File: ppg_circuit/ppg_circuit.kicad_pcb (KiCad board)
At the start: 2 copper layers, 14 parts, among them U1 Opamp_Dual, U2 MCP6001x-LT

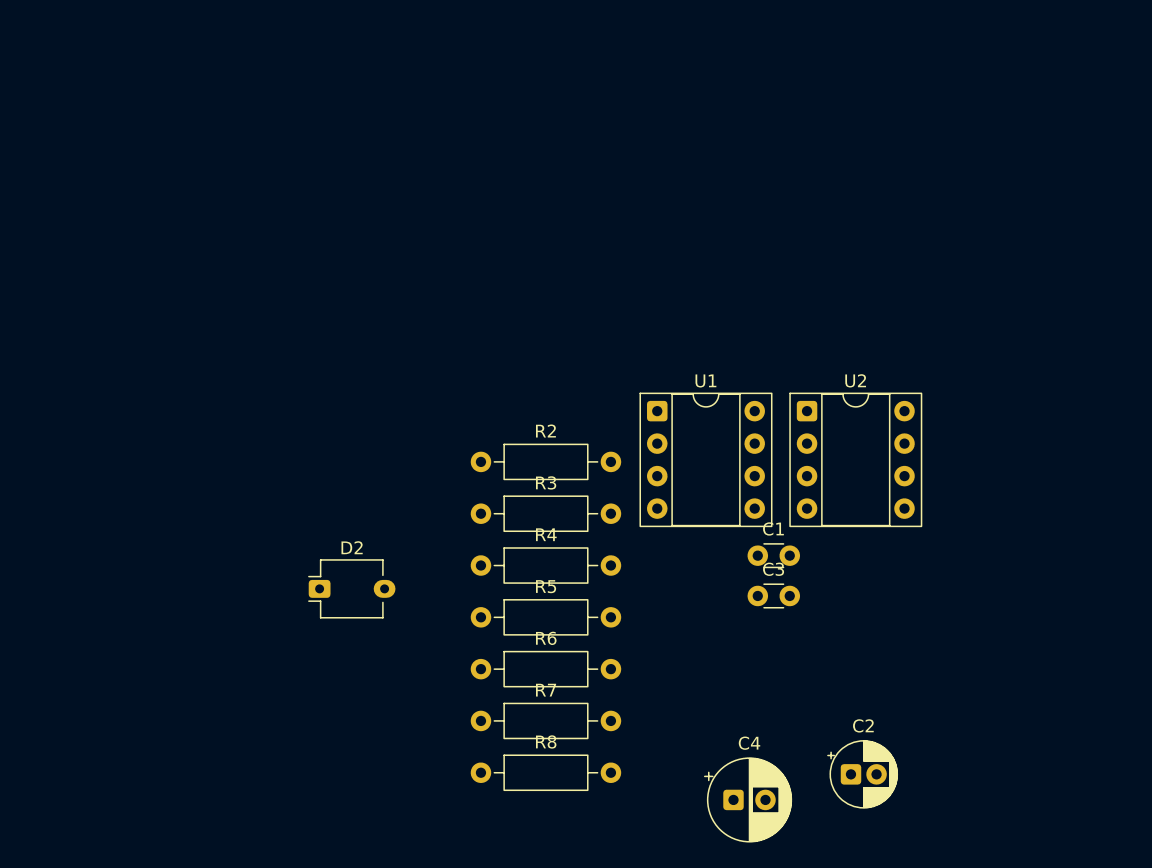
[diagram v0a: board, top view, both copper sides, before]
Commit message: designed pcb, added teensy to the design
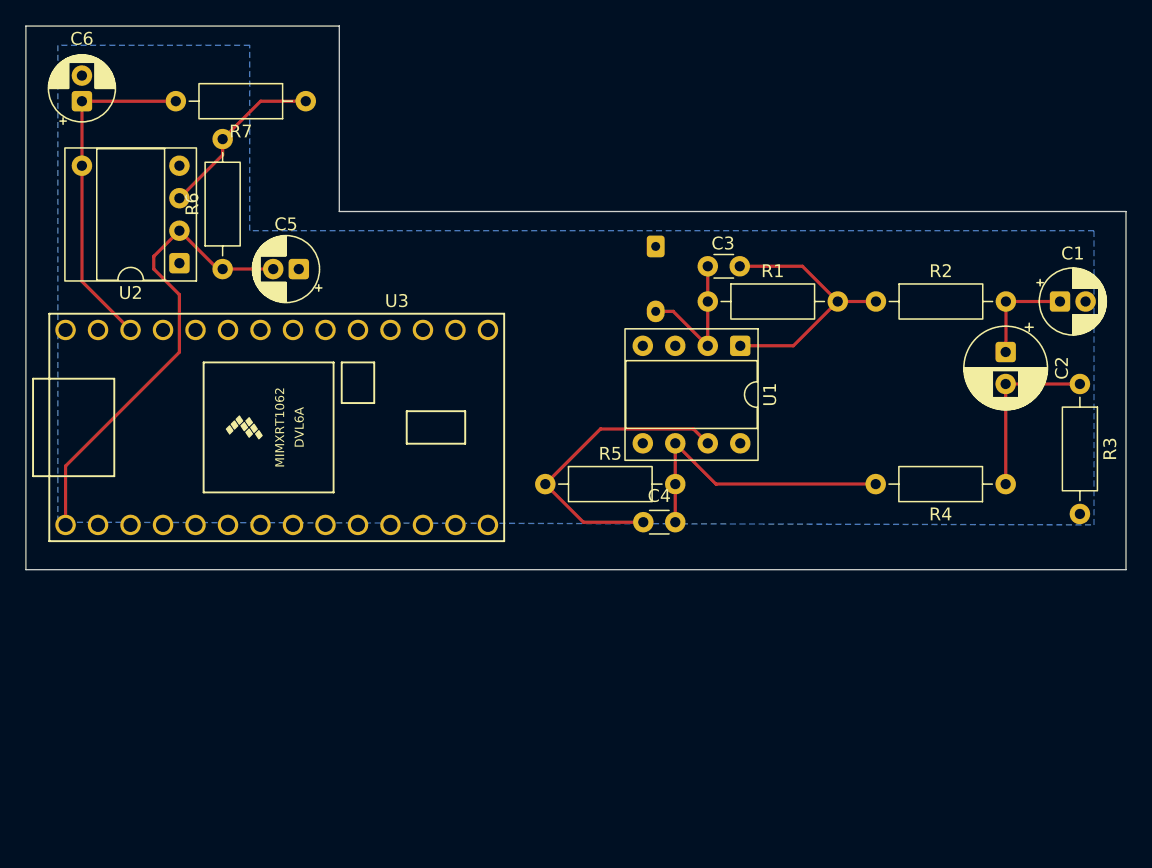
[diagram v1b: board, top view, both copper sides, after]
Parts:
- added C5: 10u, Capacitor_THT:CP_Radial_D5.0mm_P2.00mm, F.Cu at (62.3, 37.5)
- added C6: 10u, Capacitor_THT:CP_Radial_D5.0mm_P2.00mm, F.Cu at (45.4, 24.4)
- added U3: Teensy4.0, teensy:Teensy40, F.Cu at (60.6, 49.9)
- D1: renamed from D2; moved to B.Cu
- moved R7 54.3 mm to (62.9, 24.4), turned to 180 degrees
- moved U2 50.4 mm to (53.0, 37.0), turned to 180 degrees
- moved R3 50.2 mm to (123.4, 46.5), turned to -90 degrees
- moved R4 41.5 mm to (117.6, 54.3), turned to 180 degrees
- moved C2 41.0 mm to (117.6, 44.0), turned to -90 degrees
- moved R6 40.7 mm to (56.4, 37.5), turned to 90 degrees
- moved C1 40.4 mm to (121.8, 40.0)
- moved D1 37.5 mm to (90.2, 35.7), turned to -90 degrees
- moved R2 35.1 mm to (107.5, 40.0)
- moved C3 25.8 mm to (96.8, 37.3), turned to 180 degrees
- moved R1 21.7 mm to (94.3, 40.0)
- moved R5 15.3 mm to (81.6, 54.3)
- moved C4 9.32 mm to (89.3, 57.3)
- moved U1 8.26 mm to (96.8, 43.5), turned to -90 degrees
- renumbered C2 to C1, C4 to C2, C1 to C4, R2 to R1, R3 to R2, R5 to R3, R6 to R5, R7 to R6, R8 to R7
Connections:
- R6 pad 2: GND -> Net-(U2-+)
- R7 pad 1: GND -> Net-(U2-+)
- U2 pad 1: /ground -> GND
- U2 pad 3: GND -> Net-(U2-+)
- U2 pad 4: /ground -> GND
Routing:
- net /low: track 0.00 -> 36.9 mm
- net /high: track 0.00 -> 26.8 mm
- net /outf: track 0.00 -> 23.8 mm
- net Net-(U1B--): track 0.00 -> 23.2 mm
- net /out1: track 0.00 -> 20.8 mm
- net Net-(U2-+): track 0.00 -> 13.7 mm
- net /out3: track 0.00 -> 13.6 mm
- net /in: track 0.00 -> 11.4 mm
- net /out2: track 0.00 -> 8.19 mm
- added copper zone on B.Cu, net GND
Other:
- board outline added: 86 x 42.5 mm

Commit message: fixed errors in pcb and moved the photodiode so it is more accessable on the pcb
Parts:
- added REF**: MountingHole_2.2mm_M2, MountingHole:MountingHole_2.2mm_M2, F.Cu at (62.5, 29.0)
- moved D1 7.28 mm to (83.0, 35.5), turned to 0 degrees
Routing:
- net /low: track 36.9 -> 89.6 mm, vias 0 -> 1
- net /high: track 26.8 -> 78.1 mm, vias 0 -> 1
- net /outf: track 23.8 -> 38.8 mm
- net /in: track 11.4 -> 16.8 mm

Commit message: finished modular 3d design with 3 different components and added screw holes for fastening
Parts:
- removed the REF** at (62.5, 29.0)
- added REF**: MountingHole_2.2mm_M2, MountingHole:MountingHole_2.2mm_M2, F.Cu at (69.0, 37.0)
- added REF**: MountingHole_2.2mm_M2, MountingHole:MountingHole_2.2mm_M2, F.Cu at (117.5, 58.5)
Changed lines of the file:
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@@
 			(outputformat 1)
 			(mirror no)
-			(drillshape 1)
+			(drillshape 0)
 			(scaleselection 1)
-			(outputdirectory "")
+			(outputdirectory "gerber/")
 		)
 	)
@@
 		)
 	)
+	(footprint "MountingHole:MountingHole_2.2mm_M2"
+		(layer "F.Cu")
+		(at 69 37)
+		(descr "Mounting Hole 2.2mm, M2, no annular, generated by kicad-footprint-generator mountinghole.py")
+		(tags "mountinghole M2")
+		(property "Reference" "REF**"
+			(at 4.5 -2.5 0)
+			(layer "F.SilkS")
+			(effects
+				(font
+					(size 1 1)
+					(thickness 0.15)
+				)
+			)
+		)
+		(property "Value" "MountingHole_2.2mm_M2"
+			(at 0 3.15 0)
+			(layer "F.Fab")
+			(effects
+				(font
+					(size 1 1)
+					(thickness 0.15)
+				)
+			)
+		)
+		(property "Datasheet" ""
+			(at 0 0 0)
+			(layer "F.Fab")
+			(hide yes)
+			(effects
+				(font
+					(size 1.27 1.27)
+				)
+			)
+		)
+		(property "Description" ""
+			(at 0 0 0)
+			(layer "F.Fab")
+			(hide yes)
+			(effects
+				(font
+					(size 1.27 1.27)
+				)
+			)
+		)
+		(property "KiLib_Generator" "mounting_hardware/mounting_hole"
+			(at 0 0 0)
+			(layer "F.SilkS")
+			(hide yes)
+			(effects
+				(font
+					(size 1 1)
+					(thickness 0.15)
+				)
+			)
+		)
+		(attr exclude_from_pos_files exclude_from_bom)
+		(duplicate_pad_numbers_are_jumpers no)
+		(fp_circle
+			(center 0 0)
+			(end 2.2 0)
+			(stroke
+				(width 0.15)
+				(type solid)
+			)
+			(fill no)
+			(layer "Cmts.User")
+		)
+		(fp_circle
+			(center 0 0)
+			(end 2.45 0)
+			(stroke
+				(width 0.05)
+				(type solid)
+			)
+			(fill no)
+			(layer "F.CrtYd")
+		)
+		(fp_text user "${REFERENCE}"
+			(at 0 0 0)
+			(layer "F.Fab")
+			(effects
+				(font
+					(size 1 1)
+					(thickness 0.15)
+				)
+			)
+		)
+		(pad "" np_thru_hole circle
+			(at 0 0)
+			(size 2.2 2.2)
+			(drill 2.2)
+			(layers "*.Cu" "*.Mask")
+		)
+		(embedded_fonts no)
+	)
 	(footprint "Resistor_THT:R_Axial_DIN0207_L6.3mm_D2.5mm_P10.16mm_Horizontal"
 		(layer "F.Cu")
@@
 		)
 	)
-	(footprint "MountingHole:MountingHole_2.2mm_M2"
-		(layer "F.Cu")
-		(at 62.5 29)
-		(descr "Mounting Hole 2.2mm, M2, no annular, generated by kicad-footprint-generator mountinghole.py")
-		(tags "mountinghole M2")
-		(property "Reference" "REF**"
-			(at 0 -3.15 0)
-			(layer "F.SilkS")
-			(effects
-				(font
-					(size 1 1)
-					(thickness 0.15)
-				)
-			)
-		)
-		(property "Value" "MountingHole_2.2mm_M2"
-			(at 0 3.15 0)
-			(layer "F.Fab")
-			(effects
-				(font
-					(size 1 1)
-					(thickness 0.15)
-				)
-			)
-		)
-		(property "Datasheet" ""
-			(at 0 0 0)
-			(layer "F.Fab")
-			(hide yes)
-			(effects
-				(font
-					(size 1.27 1.27)
-				)
-			)
-		)
-		(property "Description" ""
-			(at 0 0 0)
-			(layer "F.Fab")
-			(hide yes)
-			(effects
-				(font
-					(size 1.27 1.27)
-				)
-			)
-		)
-		(property "KiLib_Generator" "mounting_hardware/mounting_hole"
-			(at 0 0 0)
-			(layer "F.SilkS")
-			(hide yes)
-			(effects
-				(font
-					(size 1 1)
-					(thickness 0.15)
-				)
-			)
-		)
-		(attr exclude_from_pos_files exclude_from_bom)
-		(duplicate_pad_numbers_are_jumpers no)
-		(fp_circle
-			(center 0 0)
-			(end 2.2 0)
-			(stroke
-				(width 0.15)
-				(type solid)
-			)
-			(fill no)
-			(layer "Cmts.User")
-		)
-		(fp_circle
-			(center 0 0)
-			(end 2.45 0)
-			(stroke
-				(width 0.05)
-				(type solid)
-			)
-			(fill no)
-			(layer "F.CrtYd")
-		)
-		(fp_text user "${REFERENCE}"
-			(at 0 0 0)
-			(layer "F.Fab")
-			(effects
-				(font
-					(size 1 1)
-					(thickness 0.15)
-				)
-			)
-		)
-		(pad "" np_thru_hole circle
-			(at 0 0)
-			(size 2.2 2.2)
-			(drill 2.2)
-			(layers "*.Cu" "*.Mask")
-		)
-		(embedded_fonts no)
-	)
 	(footprint "Capacitor_THT:CP_Radial_D5.0mm_P2.00mm"
 		(layer "F.Cu")
@@
 		)
 	)
+	(footprint "MountingHole:MountingHole_2.2mm_M2"
+		(layer "F.Cu")
+		(at 117.5 58.5)
+		(descr "Mounting Hole 2.2mm, M2, no annular, generated by kicad-footprint-generator mountinghole.py")
+		(tags "mountinghole M2")
+		(property "Reference" "REF**"
+			(at -5 1 0)
+			(layer "F.SilkS")
+			(effects
+				(font
+					(size 1 1)
+					(thickness 0.15)
+				)
+			)
+		)
+		(property "Value" "MountingHole_2.2mm_M2"
+			(at 0 3.15 0)
+			(layer "F.Fab")
+			(effects
+				(font
+					(size 1 1)
+					(thickness 0.15)
+				)
+			)
+		)
+		(property "Datasheet" ""
+			(at 0 0 0)
+			(layer "F.Fab")
+			(hide yes)
+			(effects
+				(font
+					(size 1.27 1.27)
+				)
+			)
+		)
+		(property "Description" ""
+			(at 0 0 0)
+			(layer "F.Fab")
+			(hide yes)
+			(effects
+				(font
+					(size 1.27 1.27)
+				)
+			)
+		)
+		(property "KiLib_Generator" "mounting_hardware/mounting_hole"
+			(at 0 0 0)
+			(layer "F.SilkS")
+			(hide yes)
+			(effects
+				(font
+					(size 1 1)
+					(thickness 0.15)
+				)
+			)
+		)
+		(attr exclude_from_pos_files exclude_from_bom)
+		(duplicate_pad_numbers_are_jumpers no)
+		(fp_circle
+			(center 0 0)
+			(end 2.2 0)
+			(stroke
+				(width 0.15)
+				(type solid)
+			)
+			(fill no)
+			(layer "Cmts.User")
+		)
+		(fp_circle
+			(center 0 0)
+			(end 2.45 0)
+			(stroke
+				(width 0.05)
+				(type solid)
+			)
+			(fill no)
+			(layer "F.CrtYd")
+		)
+		(fp_text user "${REFERENCE}"
+			(at 0 0 0)
+			(layer "F.Fab")
+			(effects
+				(font
+					(size 1 1)
+					(thickness 0.15)
+				)
+			)
+		)
+		(pad "" np_thru_hole circle
+			(at 0 0)
+			(size 2.2 2.2)
+			(drill 2.2)
+			(layers "*.Cu" "*.Mask")
+		)
+		(embedded_fonts no)
+	)
 	(footprint "Resistor_THT:R_Axial_DIN0207_L6.3mm_D2.5mm_P10.16mm_Horizontal"
 		(layer "F.Cu")
@@
 	)
 	(segment
-		(start 86 47)
+		(start 85.25 46.25)
 		(end 83.5 44.5)
 		(width 0.25)
@@
 		(width 0.25)
 		(layer "B.Cu")
+		(net "/high")
+	)
+	(segment
+		(start 86 47)
+		(end 85.25 46.25)
+		(width 0.25)
+		(layer "B.Cu")

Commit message: updated ppg pcb to fix the footprint, and updated firmware after changing pins used
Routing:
- net /low: track 89.6 -> 94.4 mm
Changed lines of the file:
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@@
 		(sheetname "/")
 		(sheetfile "ppg_circuit.kicad_sch")
-		(units
-			(unit
-				(name "A")
-				(pins "3" "4" "5" "2" "1")
-			)
-		)
 		(attr through_hole)
 		(duplicate_pad_numbers_are_jumpers no)
@@
 		)
 		(pad "2" thru_hole circle
-			(at 0 2.54 180)
+			(at -0.024677 7.72744 180)
 			(size 1.6 1.6)
 			(drill 0.8)
@@
 		)
 		(pad "4" thru_hole circle
-			(at 0 7.62 180)
+			(at 0 2.5 180)
 			(size 1.6 1.6)
 			(drill 0.8)
@@
 	)
 	(segment
-		(start 81 46)
-		(end 81 49)
+		(start 44.1 52.9)
+		(end 44.1 57.5)
 		(width 0.25)
 		(layer "F.Cu")
@@
 	)
 	(segment
-		(start 51 36.5)
-		(end 53 34.5)
+		(start 51 31.337237)
+		(end 51 37.5)
 		(width 0.25)
 		(layer "F.Cu")
@@
 	(segment
 		(start 53 44)
-		(end 53 41)
+		(end 44.1 52.9)
 		(width 0.25)
 		(layer "F.Cu")
@@
 	)
 	(segment
-		(start 44.1 57.5)
-		(end 44.1 52.9)
+		(start 81 46)
+		(end 81 49)
 		(width 0.25)
 		(layer "F.Cu")
@@
 	)
 	(segment
-		(start 51 37.5)
-		(end 51 36.5)
+		(start 56.38 37.5)
+		(end 55 37.5)
 		(width 0.25)
 		(layer "F.Cu")
@@
 	)
 	(segment
-		(start 60.335113 37.5)
-		(end 56.38 37.5)
+		(start 53 39.5)
+		(end 53 44)
 		(width 0.25)
 		(layer "F.Cu")
@@
 	)
 	(segment
-		(start 56 37.5)
-		(end 53 34.5)
+		(start 55 37.5)
+		(end 53 39.5)
 		(width 0.25)
 		(layer "F.Cu")
@@
 	)
 	(segment
-		(start 89.225219 43.5)
-		(end 83.5 43.5)
+		(start 53.024677 29.31256)
+		(end 51 31.337237)
 		(width 0.25)
 		(layer "F.Cu")
@@
 	)
 	(segment
-		(start 56.38 37.5)
-		(end 56 37.5)
+		(start 60.335113 37.5)
+		(end 56.38 37.5)
 		(width 0.25)
 		(layer "F.Cu")
@@
 	)
 	(segment
-		(start 53 41)
-		(end 53 39.5)
+		(start 89.225219 43.5)
+		(end 83.5 43.5)
 		(width 0.25)
 		(layer "F.Cu")
@@
 	)
 	(segment
-		(start 44.1 52.9)
-		(end 53 44)
+		(start 51 37.5)
+		(end 53 39.5)
 		(width 0.25)
 		(layer "F.Cu")
@@
 		(width 0.25)
 		(layer "F.Cu")
-		(net "/low")
-	)
-	(segment
-		(start 53 39.5)
-		(end 51 37.5)
-		(width 0.25)
-		(layer "F.Cu")
